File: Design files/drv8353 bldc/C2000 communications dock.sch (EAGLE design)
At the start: 3 parts, among them IC1 ADUM1311ARWZ, J3 SS-6488-NF-A431

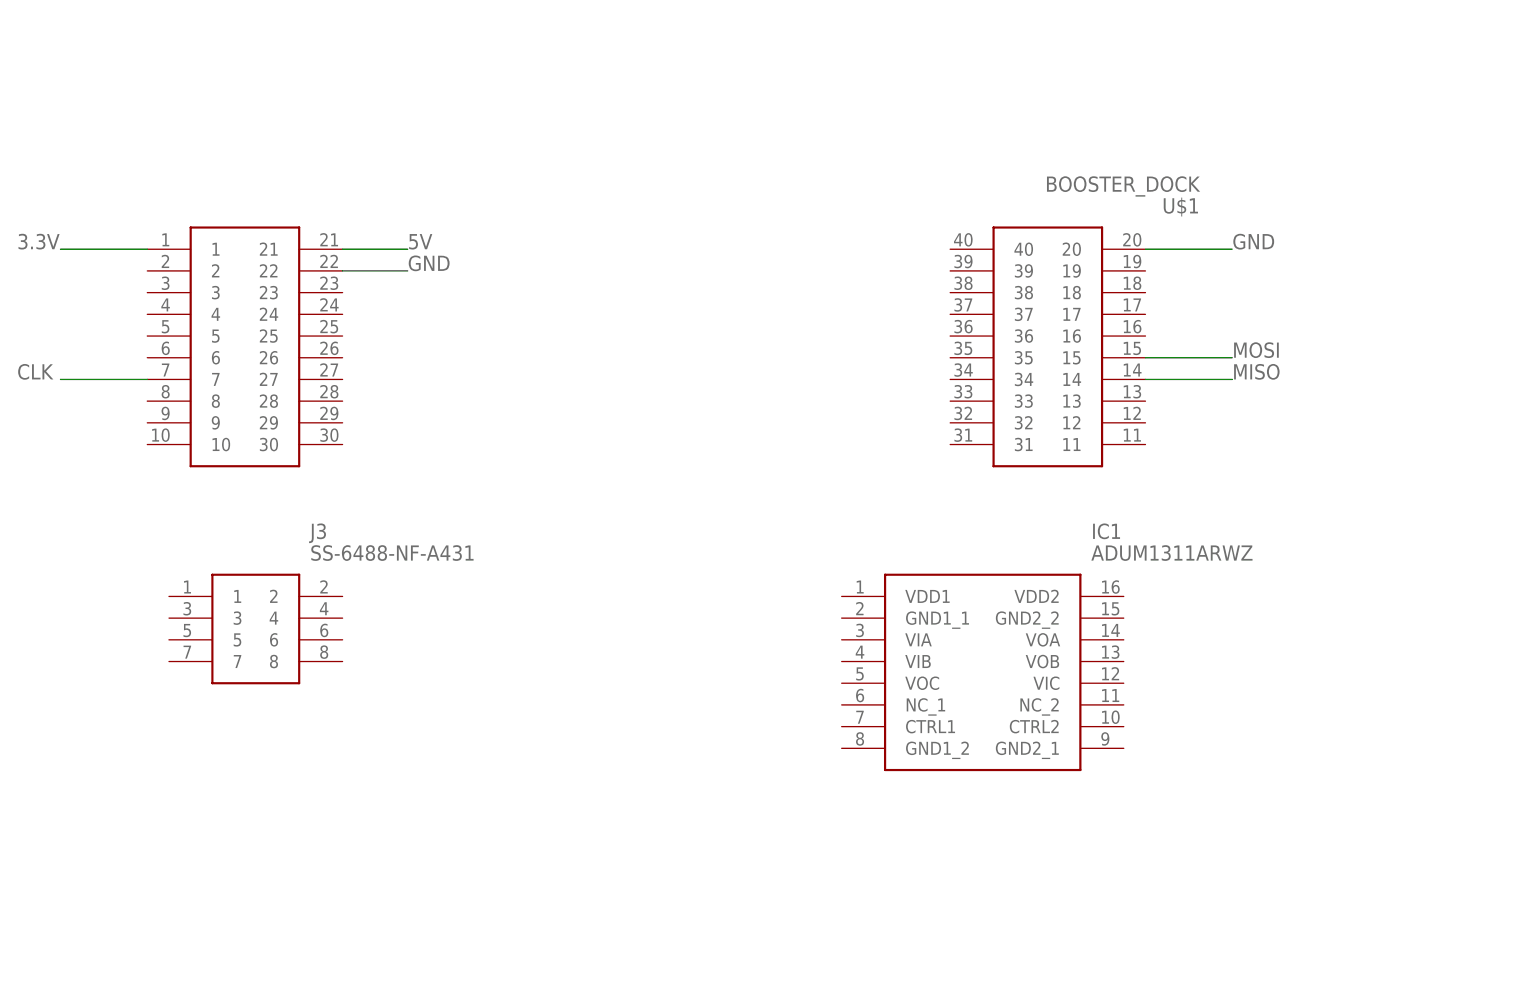
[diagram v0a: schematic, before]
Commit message: did some wiring and added led's
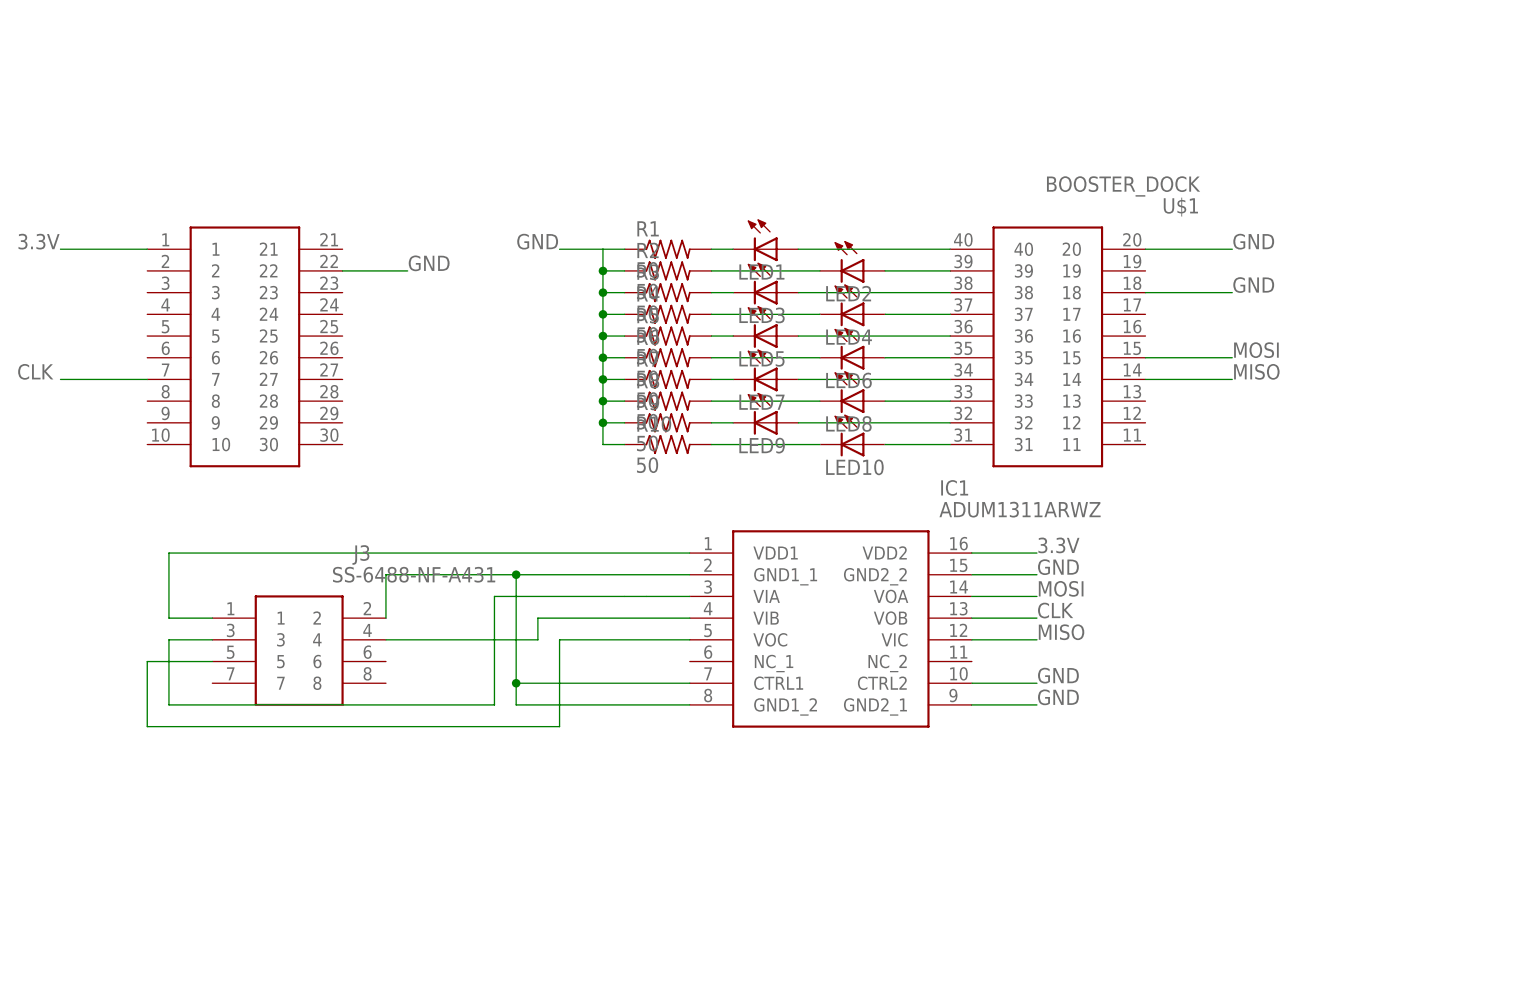
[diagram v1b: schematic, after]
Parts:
- added LED1, LED10, LED2, LED3, LED4, LED5, LED6, LED7, LED8, LED9: (no value), eagle-ltspice:LED_ESML0603
- added R1, R10, R2, R3, R4, R5, R6, R7, R8, R9: 50, rcl:R-US_R0603
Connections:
- removed net 5V: U$1.21
- new net N$1: IC1.VIA, J3.3
- new net N$10: IC1.VDD1, J3.1
- new net N$11: LED8.A, U$1.33
- new net N$12: LED9.A, U$1.32
- new net N$13: IC1.VIB, J3.4
- new net N$14: IC1.VOC, J3.5
- new net N$15: LED10.A, U$1.31
- new net N$16: IC1.CTRL1, IC1.GND1_1, IC1.GND1_2, J3.2
- new net N$17: LED1.C, R1.2
- new net N$18: LED2.C, R2.2
- new net N$19: LED3.C, R3.2
- new net N$2: LED1.A, U$1.40
- new net N$20: LED4.C, R4.2
- new net N$21: LED5.C, R5.2
- new net N$22: LED6.C, R6.2
- new net N$23: LED7.C, R7.2
- new net N$24: LED8.C, R8.2
- new net N$25: LED9.C, R9.2
- new net N$26: LED10.C, R10.2
- new net N$3: LED2.A, U$1.39
- new net N$4: LED3.A, U$1.38
- new net N$5: LED4.A, U$1.37
- new net N$6: LED5.A, U$1.36
- new net N$8: LED6.A, U$1.35
- new net N$9: LED7.A, U$1.34
- net 3.3V: now also IC1.VDD2
- net CLK: now also IC1.VOB
- net GND: now also IC1.CTRL2, IC1.GND2_1, IC1.GND2_2, R1.1, R10.1, R2.1, R3.1, R4.1, R5.1, R6.1, R7.1, R8.1, R9.1, U$1.18
- net MISO: now also IC1.VIC
- net MOSI: now also IC1.VOA
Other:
- moved on the sheet: IC1, J3

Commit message: added pot, and headers for spi , i2c, analog pins, and the input spi signal
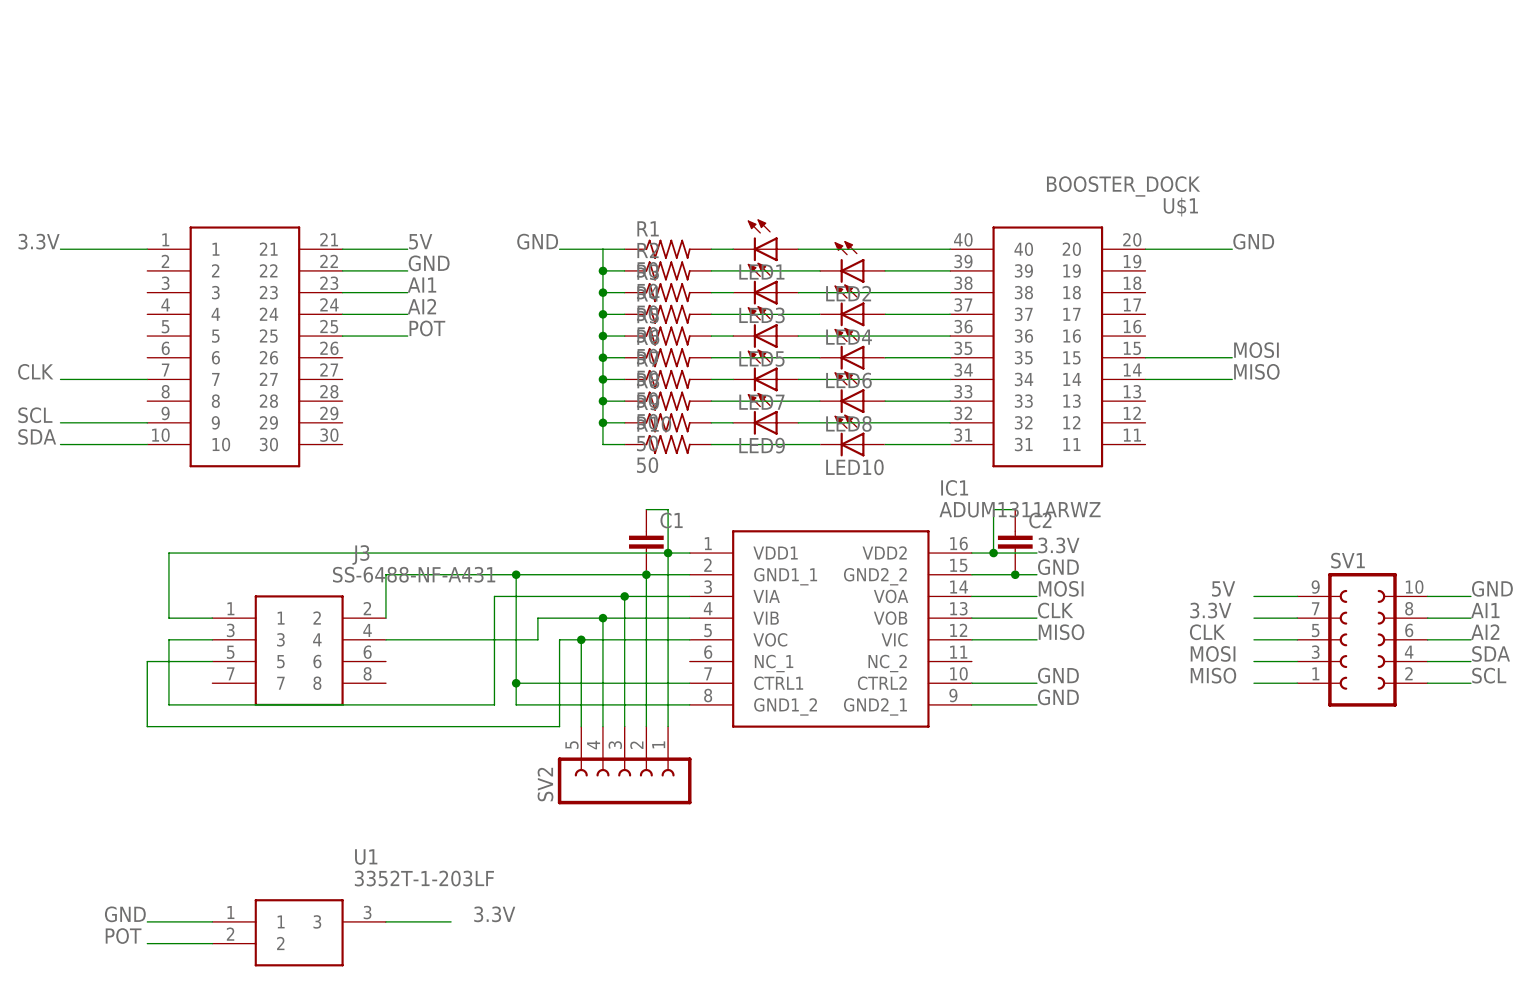
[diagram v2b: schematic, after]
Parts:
- added C1, C2: (no value), rcl:C-EUC0603
- added SV1: (no value), con-lsta:FE05-2
- added SV2: (no value), con-lsta:FE05-1
- added U1: 3352T-1-203LF, SamacSys_Parts:3352T-1-203LF
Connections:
- new net 5V: SV1.9, U$1.21
- new net AI1: SV1.8, U$1.23
- new net AI2: SV1.6, U$1.24
- new net POT: U$1.25, U1.2
- new net SCL: SV1.2, U$1.9
- new net SDA: SV1.4, U$1.10
- net 3.3V: now also C2.1, SV1.7, U1.3
- net CLK: now also SV1.5
- net GND: now also C2.2, SV1.10, U1.1; no longer U$1.18
- net MISO: now also SV1.1
- net MOSI: now also SV1.3
- net N$1: now also SV2.3
- net N$10: now also C1.1, SV2.1
- net N$13: now also SV2.4
- net N$14: now also SV2.5
- net N$16: now also C1.2, SV2.2

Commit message: reordered header and did a tenative layout
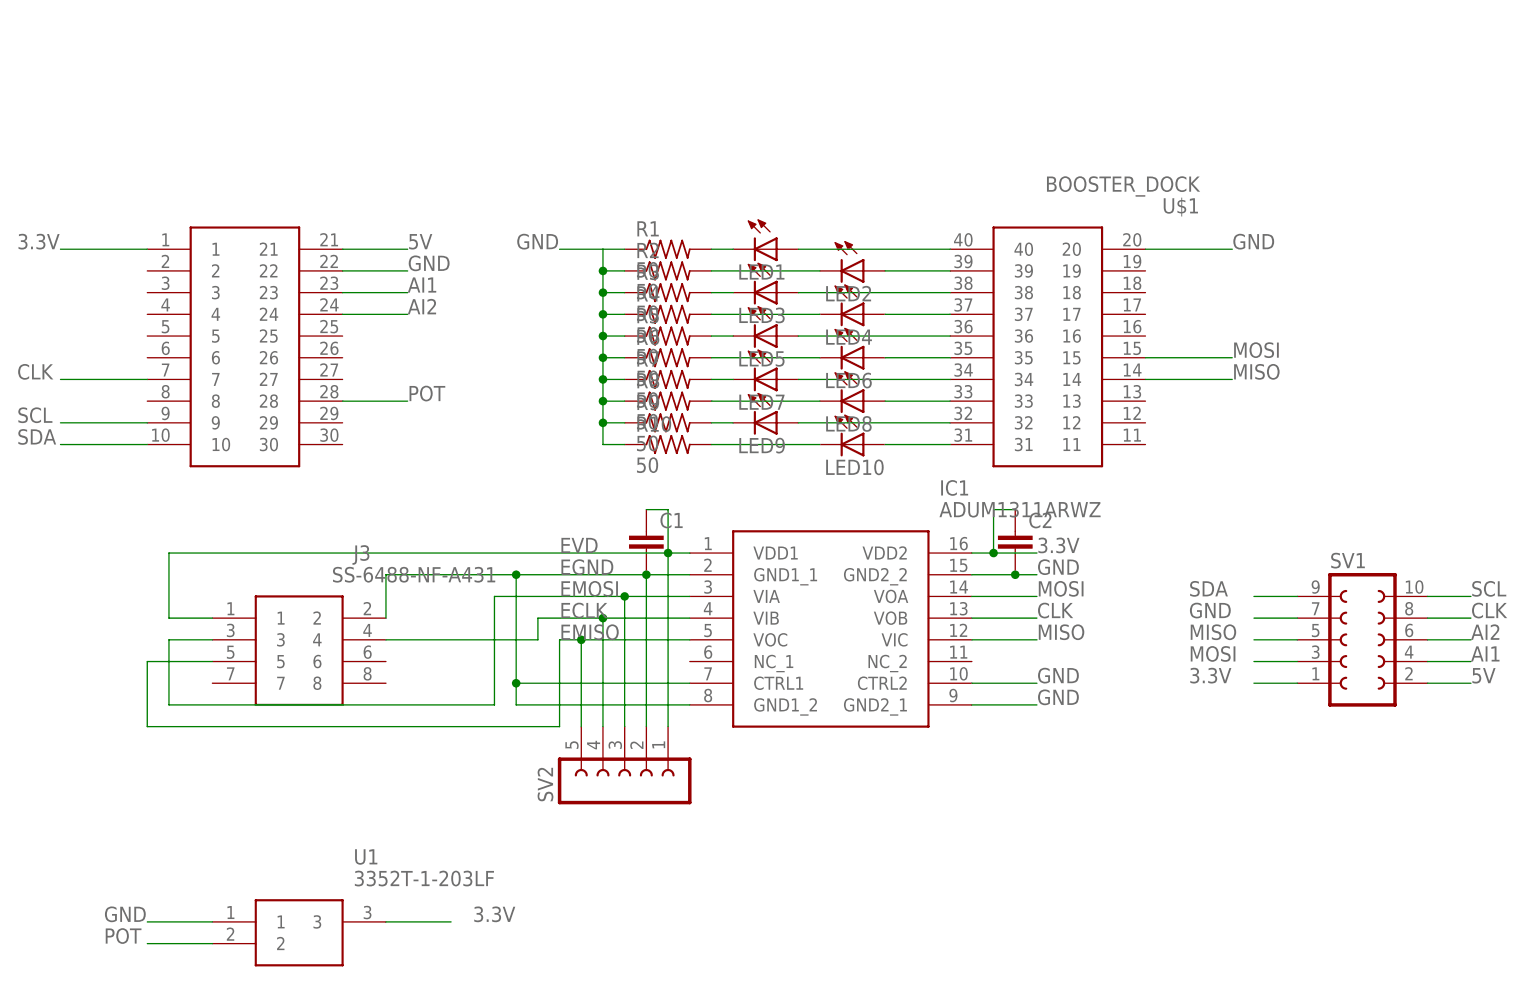
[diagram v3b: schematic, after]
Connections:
- net N$1 renamed EMOSI
- net N$10 renamed EVD
- net N$13 renamed ECLK
- net N$14 renamed EMISO
- net N$16 renamed EGND
- net 3.3V: now also SV1.1; no longer SV1.7
- net 5V: now also SV1.2; no longer SV1.9
- net AI1: now also SV1.4; no longer SV1.8
- net CLK: now also SV1.8; no longer SV1.5
- net GND: now also SV1.7; no longer SV1.10
- net MISO: now also SV1.5; no longer SV1.1
- net POT: now also U$1.28; no longer U$1.25
- net SCL: now also SV1.10; no longer SV1.2
- net SDA: now also SV1.9; no longer SV1.4
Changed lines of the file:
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@@
-</segment>
-<segment>
-<pinref part="SV1" gate="G$1" pin="7"/>
-<wire x1="129.54" y1="17.78" x2="124.46" y2="17.78" width="0.1524" layer="91"/>
-<label x="116.84" y="17.78" size="1.778" layer="95"/>
 </segment>
 <segment>
@@
 <wire x1="22.86" y1="-17.78" x2="30.48" y2="-17.78" width="0.1524" layer="91"/>
 <label x="33.02" y="-17.78" size="1.778" layer="95"/>
+</segment>
+<segment>
+<pinref part="SV1" gate="G$1" pin="1"/>
+<wire x1="129.54" y1="10.16" x2="124.46" y2="10.16" width="0.1524" layer="91"/>
+<label x="116.84" y="10.16" size="1.778" layer="95"/>
 </segment>
 </net>
@@
 </segment>
 <segment>
-<pinref part="SV1" gate="G$1" pin="10"/>
-<wire x1="144.78" y1="20.32" x2="149.86" y2="20.32" width="0.1524" layer="91"/>
-<label x="149.86" y="20.32" size="1.778" layer="95"/>
-</segment>
-<segment>
 <pinref part="U1" gate="G$1" pin="1"/>
 <wire x1="2.54" y1="-17.78" x2="-5.08" y2="-17.78" width="0.1524" layer="91"/>
 <label x="-10.16" y="-17.78" size="1.778" layer="95"/>
 </segment>
+<segment>
+<pinref part="SV1" gate="G$1" pin="7"/>
+<wire x1="129.54" y1="17.78" x2="124.46" y2="17.78" width="0.1524" layer="91"/>
+<label x="116.84" y="17.78" size="1.778" layer="95"/>
+</segment>
 </net>
 <net name="MISO" class="0">
@@
 </segment>
 <segment>
-<pinref part="SV1" gate="G$1" pin="1"/>
-<wire x1="129.54" y1="10.16" x2="124.46" y2="10.16" width="0.1524" layer="91"/>
-<label x="116.84" y="10.16" size="1.778" layer="95"/>
+<pinref part="SV1" gate="G$1" pin="5"/>
+<wire x1="129.54" y1="15.24" x2="124.46" y2="15.24" width="0.1524" layer="91"/>
+<label x="116.84" y="15.24" size="1.778" layer="95"/>
 </segment>
 </net>
@@
 </segment>
 <segment>
-<pinref part="SV1" gate="G$1" pin="5"/>
-<wire x1="129.54" y1="15.24" x2="124.46" y2="15.24" width="0.1524" layer="91"/>
-<label x="116.84" y="15.24" size="1.778" layer="95"/>
-</segment>
-</net>
-<net name="N$10" class="0">
+<pinref part="SV1" gate="G$1" pin="8"/>
+<wire x1="144.78" y1="17.78" x2="149.86" y2="17.78" width="0.1524" layer="91"/>
+<label x="149.86" y="17.78" size="1.778" layer="95"/>
+</segment>
+</net>
+<net name="EVD" class="0">
 <segment>
 <pinref part="IC1" gate="G$1" pin="VDD1"/>
@@
 <pinref part="SV2" gate="G$1" pin="1"/>
 <wire x1="55.88" y1="5.08" x2="55.88" y2="25.4" width="0.1524" layer="91"/>
-</segment>
-</net>
-<net name="N$13" class="0">
+<label x="43.18" y="25.4" size="1.778" layer="95"/>
+</segment>
+</net>
+<net name="ECLK" class="0">
 <segment>
 <pinref part="IC1" gate="G$1" pin="VIB"/>
@@
 <wire x1="48.26" y1="5.08" x2="48.26" y2="17.78" width="0.1524" layer="91"/>
 <junction x="48.26" y="17.78"/>
-</segment>
-</net>
-<net name="N$14" class="0">
+<label x="43.18" y="17.78" size="1.778" layer="95"/>
+</segment>
+</net>
+<net name="EMISO" class="0">
 <segment>
 <pinref part="IC1" gate="G$1" pin="VOC"/>
@@
 <wire x1="45.72" y1="5.08" x2="45.72" y2="15.24" width="0.1524" layer="91"/>
 <junction x="45.72" y="15.24"/>
-</segment>
-</net>
-<net name="N$16" class="0">
+<label x="43.18" y="15.24" size="1.778" layer="95"/>
+</segment>
+</net>
+<net name="EGND" class="0">
 <segment>
 <pinref part="IC1" gate="G$1" pin="CTRL1"/>
@@
 <pinref part="SV2" gate="G$1" pin="2"/>
 <wire x1="53.34" y1="5.08" x2="53.34" y2="22.86" width="0.1524" layer="91"/>
-</segment>
-</net>
-<net name="N$1" class="0">
+<label x="43.18" y="22.86" size="1.778" layer="95"/>
+</segment>
+</net>
+<net name="EMOSI" class="0">
 <segment>
 <pinref part="J3" gate="G$1" pin="3"/>
@@
 <wire x1="50.8" y1="5.08" x2="50.8" y2="20.32" width="0.1524" layer="91"/>
 <junction x="50.8" y="20.32"/>
+<label x="43.18" y="20.32" size="1.778" layer="95"/>
 </segment>
 </net>
@@
 </segment>
 <segment>
+<pinref part="SV1" gate="G$1" pin="10"/>
+<wire x1="144.78" y1="20.32" x2="149.86" y2="20.32" width="0.1524" layer="91"/>
+<label x="149.86" y="20.32" size="1.778" layer="95"/>
+</segment>
+</net>
+<net name="SDA" class="0">
+<segment>
+<pinref part="U$1" gate="G$1" pin="10"/>
+<wire x1="-5.08" y1="38.1" x2="-15.24" y2="38.1" width="0.1524" layer="91"/>
+<label x="-20.32" y="38.1" size="1.778" layer="95"/>
+</segment>
+<segment>
+<pinref part="SV1" gate="G$1" pin="9"/>
+<wire x1="129.54" y1="20.32" x2="124.46" y2="20.32" width="0.1524" layer="91"/>
+<label x="116.84" y="20.32" size="1.778" layer="95"/>
+</segment>
+</net>
+<net name="5V" class="0">
+<segment>
+<pinref part="U$1" gate="G$1" pin="21"/>
+<wire x1="17.78" y1="60.96" x2="25.4" y2="60.96" width="0.1524" layer="91"/>
+<label x="25.4" y="60.96" size="1.778" layer="95"/>
+</segment>
+<segment>
 <pinref part="SV1" gate="G$1" pin="2"/>
 <wire x1="144.78" y1="10.16" x2="149.86" y2="10.16" width="0.1524" layer="91"/>
@@
 </segment>
 </net>
-<net name="SDA" class="0">
-<segment>
-<pinref part="U$1" gate="G$1" pin="10"/>
-<wire x1="-5.08" y1="38.1" x2="-15.24" y2="38.1" width="0.1524" layer="91"/>
-<label x="-20.32" y="38.1" size="1.778" layer="95"/>
+<net name="AI1" class="0">
+<segment>
+<pinref part="U$1" gate="G$1" pin="23"/>
+<wire x1="17.78" y1="55.88" x2="25.4" y2="55.88" width="0.1524" layer="91"/>
+<label x="25.4" y="55.88" size="1.778" layer="95"/>
 </segment>
 <segment>
@@
 </segment>
 </net>
-<net name="5V" class="0">
-<segment>
-<pinref part="SV1" gate="G$1" pin="9"/>
-<wire x1="129.54" y1="20.32" x2="124.46" y2="20.32" width="0.1524" layer="91"/>
-<label x="119.38" y="20.32" size="1.778" layer="95"/>
-</segment>
-<segment>
-<pinref part="U$1" gate="G$1" pin="21"/>
-<wire x1="17.78" y1="60.96" x2="25.4" y2="60.96" width="0.1524" layer="91"/>
-<label x="25.4" y="60.96" size="1.778" layer="95"/>
-</segment>
-</net>
-<net name="AI1" class="0">
-<segment>
-<pinref part="U$1" gate="G$1" pin="23"/>
-<wire x1="17.78" y1="55.88" x2="25.4" y2="55.88" width="0.1524" layer="91"/>
-<label x="25.4" y="55.88" size="1.778" layer="95"/>
-</segment>
-<segment>
-<pinref part="SV1" gate="G$1" pin="8"/>
-<wire x1="144.78" y1="17.78" x2="149.86" y2="17.78" width="0.1524" layer="91"/>
-<label x="149.86" y="17.78" size="1.778" layer="95"/>
-</segment>
-</net>
 <net name="AI2" class="0">
 <segment>
@@
 </segment>
 <segment>
-<pinref part="U$1" gate="G$1" pin="25"/>
-<wire x1="17.78" y1="50.8" x2="25.4" y2="50.8" width="0.1524" layer="91"/>
-<label x="25.4" y="50.8" size="1.778" layer="95"/>
-</segment>
-</net>
+<pinref part="U$1" gate="G$1" pin="28"/>
+<wire x1="17.78" y1="43.18" x2="25.4" y2="43.18" width="0.1524" layer="91"/>
+<label x="25.4" y="43.18" size="1.778" layer="95"/>
+</segment>
+</net>
